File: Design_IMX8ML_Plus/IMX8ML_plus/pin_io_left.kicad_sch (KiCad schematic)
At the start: 4 parts, among them J1 Back_Right, J2 Front_Right

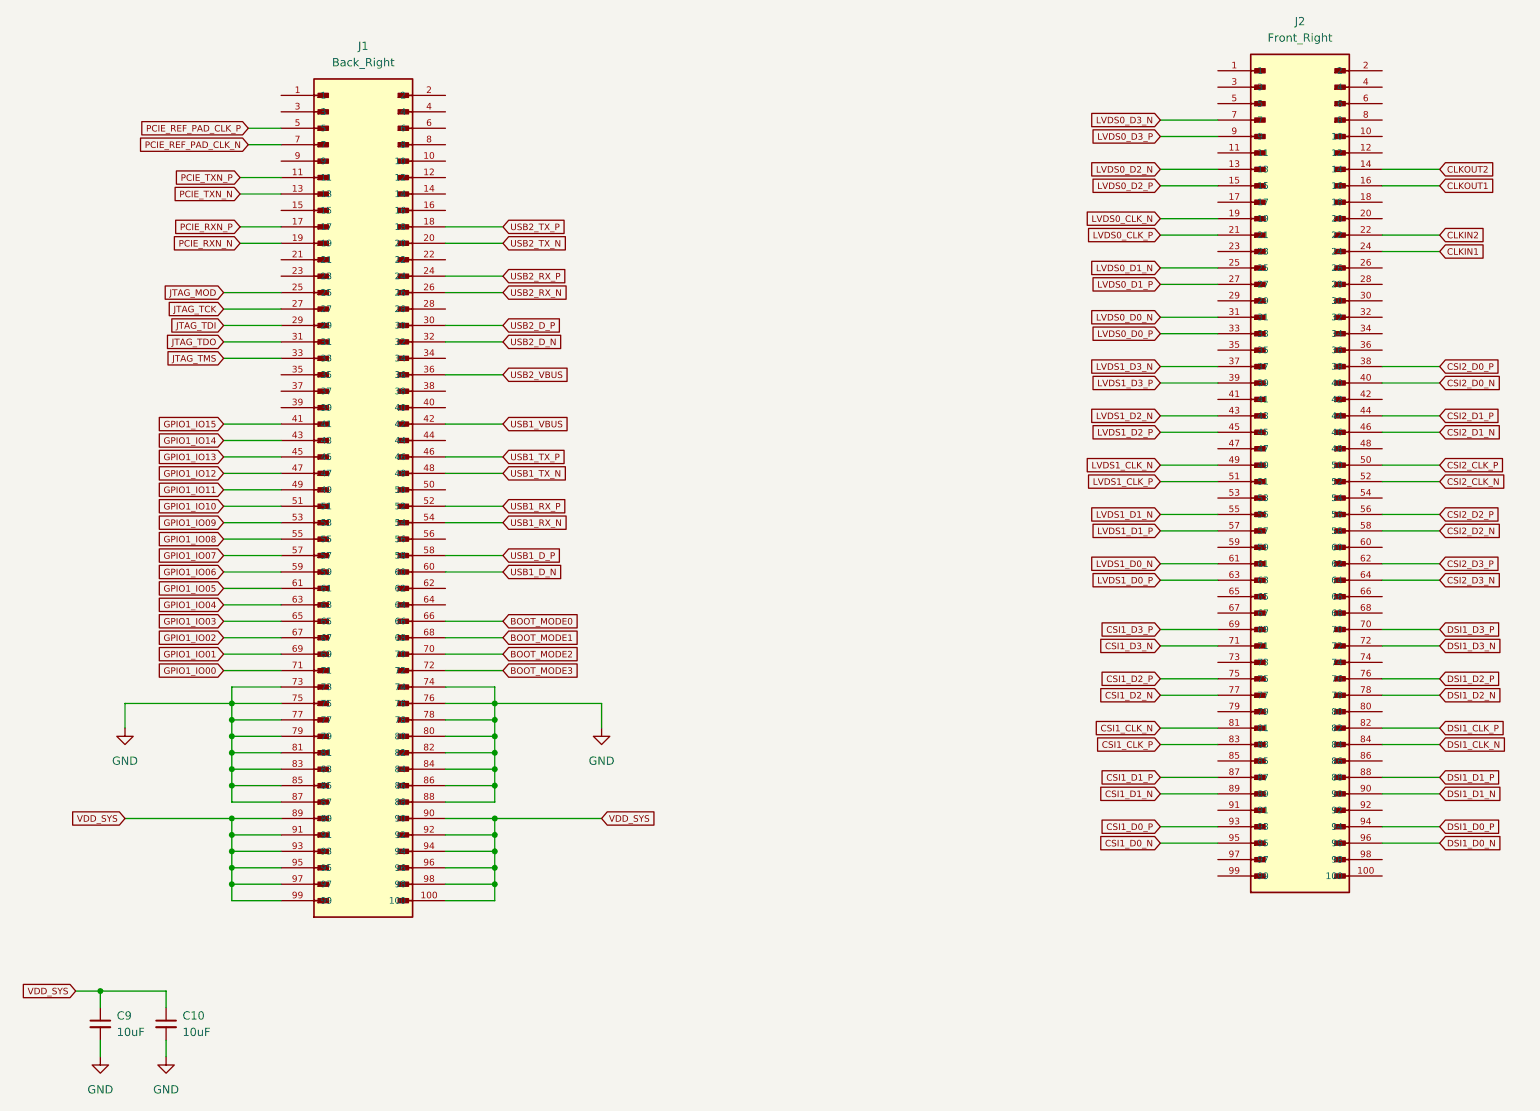
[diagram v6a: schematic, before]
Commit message: [PROCESSOR] Create zones It added power zones in the four layer
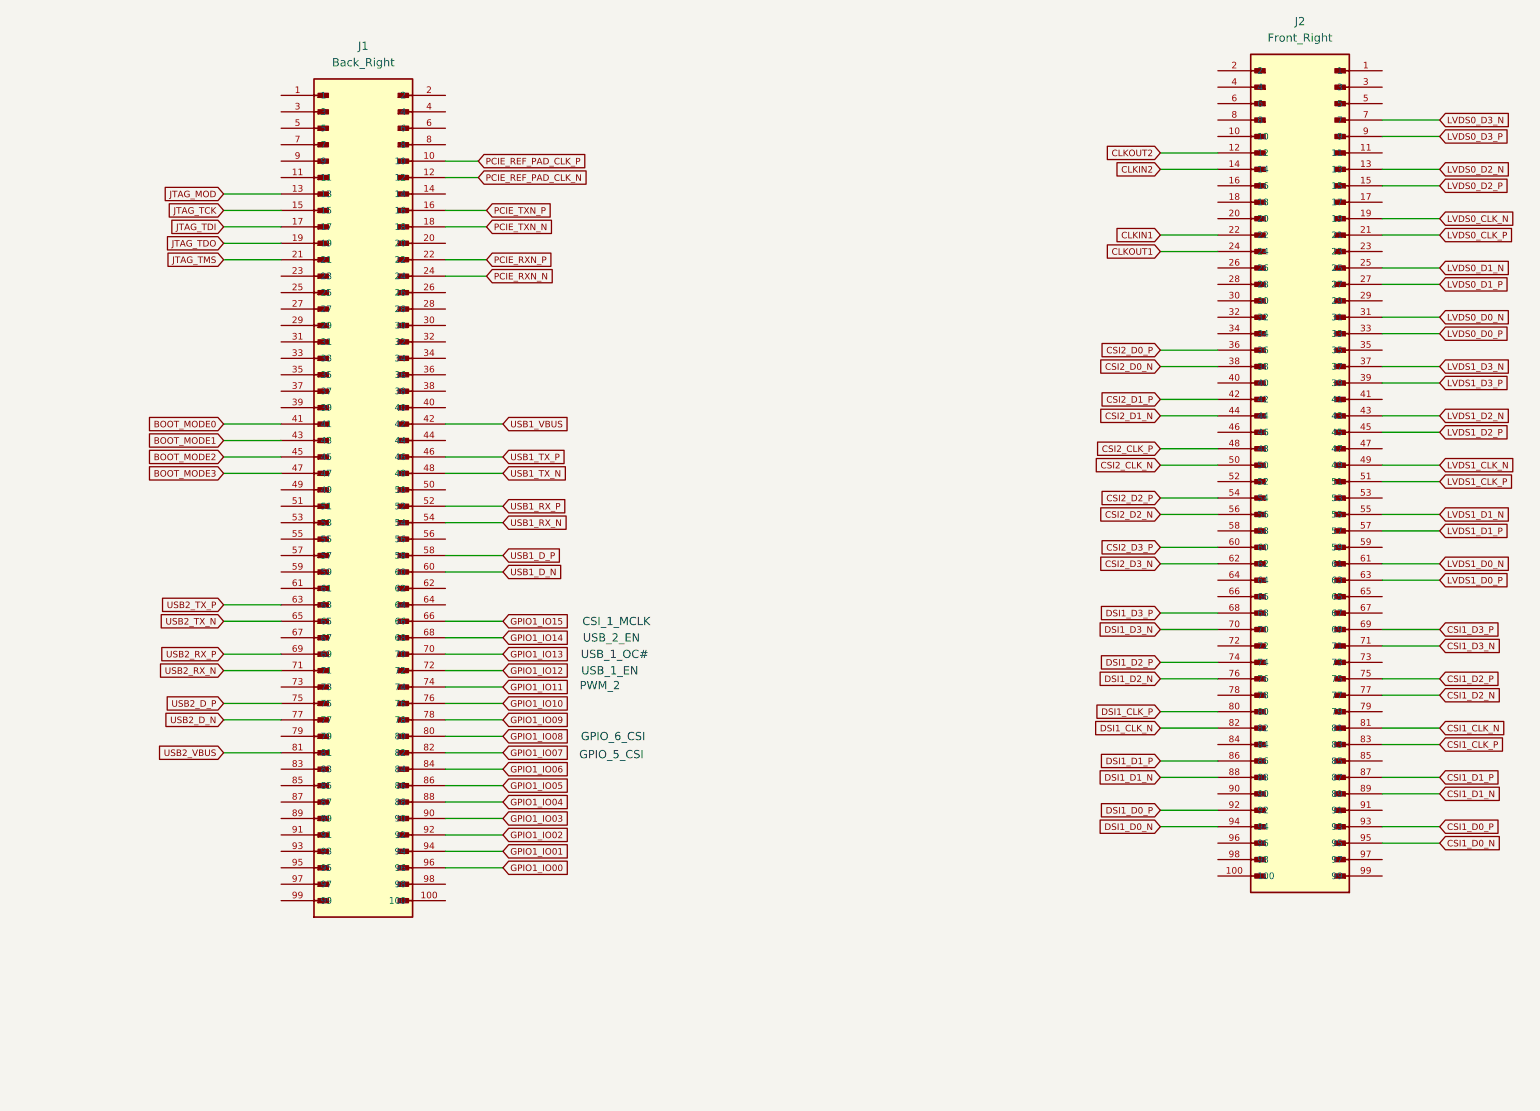
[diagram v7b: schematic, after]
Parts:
- removed C10, C9: 10uF, Capacitor_SMD:C_0201_0603Metric_Pad0.64x0.40mm_HandSolder, symbol Device:C_Small
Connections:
- net BOOT_MODE0: now also J1.41; no longer J1.66
- net BOOT_MODE1: now also J1.43; no longer J1.68
- net BOOT_MODE2: now also J1.45; no longer J1.70
- net BOOT_MODE3: now also J1.47; no longer J1.72
- net CLKIN1: now also J2.22; no longer J2.24
- net CLKIN2: now also J2.14; no longer J2.22
- net CLKOUT1: now also J2.24; no longer J2.16
- net CLKOUT2: now also J2.12; no longer J2.14
- net CSI2_CLK_N: now also J2.50; no longer J2.52
- net CSI2_CLK_P: now also J2.48; no longer J2.50
- net CSI2_D0_N: now also J2.38; no longer J2.40
- net CSI2_D0_P: now also J2.36; no longer J2.38
- net CSI2_D1_N: now also J2.44; no longer J2.46
- net CSI2_D1_P: now also J2.42; no longer J2.44
- net CSI2_D2_N: now also J2.56; no longer J2.58
- net CSI2_D2_P: now also J2.54; no longer J2.56
- net CSI2_D3_N: now also J2.62; no longer J2.64
- net CSI2_D3_P: now also J2.60; no longer J2.62
- net DSI1_CLK_N: now also J2.82; no longer J2.84
- net DSI1_CLK_P: now also J2.80; no longer J2.82
- net DSI1_D0_N: now also J2.94; no longer J2.96
- net DSI1_D0_P: now also J2.92; no longer J2.94
- net DSI1_D1_N: now also J2.88; no longer J2.90
- net DSI1_D1_P: now also J2.86; no longer J2.88
- net DSI1_D2_N: now also J2.76; no longer J2.78
- net DSI1_D2_P: now also J2.74; no longer J2.76
- net DSI1_D3_N: now also J2.70; no longer J2.72
- net DSI1_D3_P: now also J2.68; no longer J2.70
- net GPIO1_IO00: now also J1.96; no longer J1.71
- net GPIO1_IO01: now also J1.94; no longer J1.69
- net GPIO1_IO02: now also J1.92; no longer J1.67
- net GPIO1_IO03: now also J1.90; no longer J1.65
- net GPIO1_IO04: now also J1.88; no longer J1.63
- net GPIO1_IO05: now also J1.86; no longer J1.61
- net GPIO1_IO06: now also J1.84; no longer J1.59
- net GPIO1_IO07: now also J1.82; no longer J1.57
- net GPIO1_IO08: now also J1.80; no longer J1.55
- net GPIO1_IO09: now also J1.78; no longer J1.53
- net GPIO1_IO10: now also J1.76; no longer J1.51
- net GPIO1_IO11: now also J1.74; no longer J1.49
- net GPIO1_IO12: now also J1.72; no longer J1.47
- net GPIO1_IO13: now also J1.70; no longer J1.45
- net GPIO1_IO14: now also J1.68; no longer J1.43
- net GPIO1_IO15: now also J1.66; no longer J1.41
- net JTAG_MOD: now also J1.13; no longer J1.25
- net JTAG_TCK: now also J1.15; no longer J1.27
- net JTAG_TDI: now also J1.17; no longer J1.29
- net JTAG_TDO: now also J1.19; no longer J1.31
- net JTAG_TMS: now also J1.21; no longer J1.33
- net PCIE_REF_PAD_CLK_N: now also J1.12; no longer J1.7
- net PCIE_REF_PAD_CLK_P: now also J1.10; no longer J1.5
- net PCIE_RXN_N: now also J1.24; no longer J1.19
- net PCIE_RXN_P: now also J1.22; no longer J1.17
- net PCIE_TXN_N: now also J1.18; no longer J1.13
- net PCIE_TXN_P: now also J1.16; no longer J1.11
- net USB2_D_N: now also J1.77; no longer J1.32
- net USB2_D_P: now also J1.75; no longer J1.30
- net USB2_RX_N: now also J1.71; no longer J1.26
- net USB2_RX_P: now also J1.69; no longer J1.24
- net USB2_TX_N: now also J1.65; no longer J1.20
- net USB2_TX_P: now also J1.63; no longer J1.18
- net USB2_VBUS: now also J1.81; no longer J1.36
- removed net GND: J1.73, J1.74, J1.75, J1.76, J1.77, J1.78, J1.79, J1.80, J1.81, J1.82, J1.83, J1.84, J1.85, J1.86, J1.87, J1.88
- removed net VDD_SYS: J1.100, J1.89, J1.90, J1.91, J1.92, J1.93, J1.94, J1.95, J1.96, J1.97, J1.98, J1.99
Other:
- note added: "CSI_1_MCLK"
- note added: "GPIO_5_CSI"
- note added: "GPIO_6_CSI"
- note added: "PWM_2"
- note added: "USB_1_EN"
- note added: "USB_1_OC#"
- note added: "USB_2_EN"

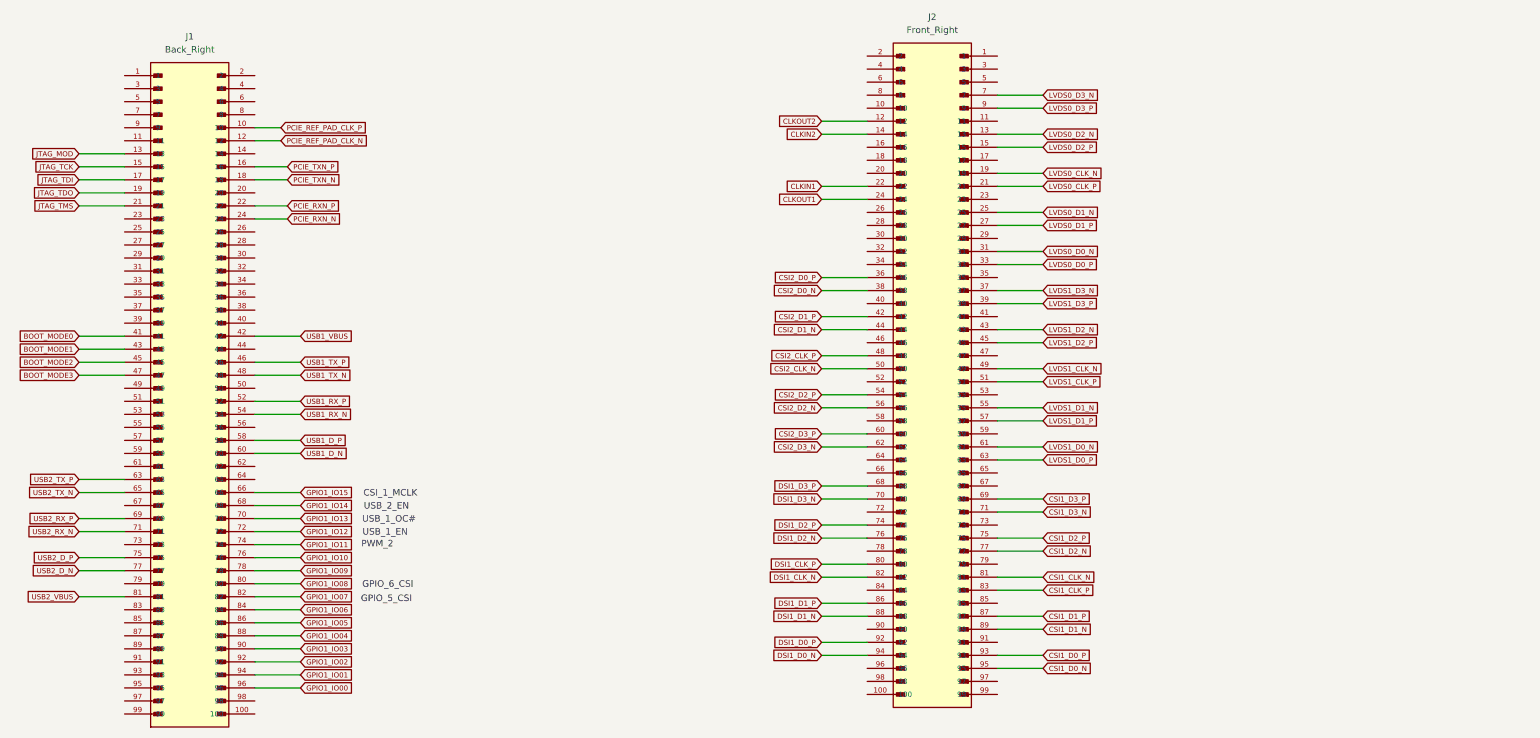
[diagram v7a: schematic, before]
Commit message: [CPU/BB] Improving the conection between the cpu and BB
* Reorganization of the components in the Base board.
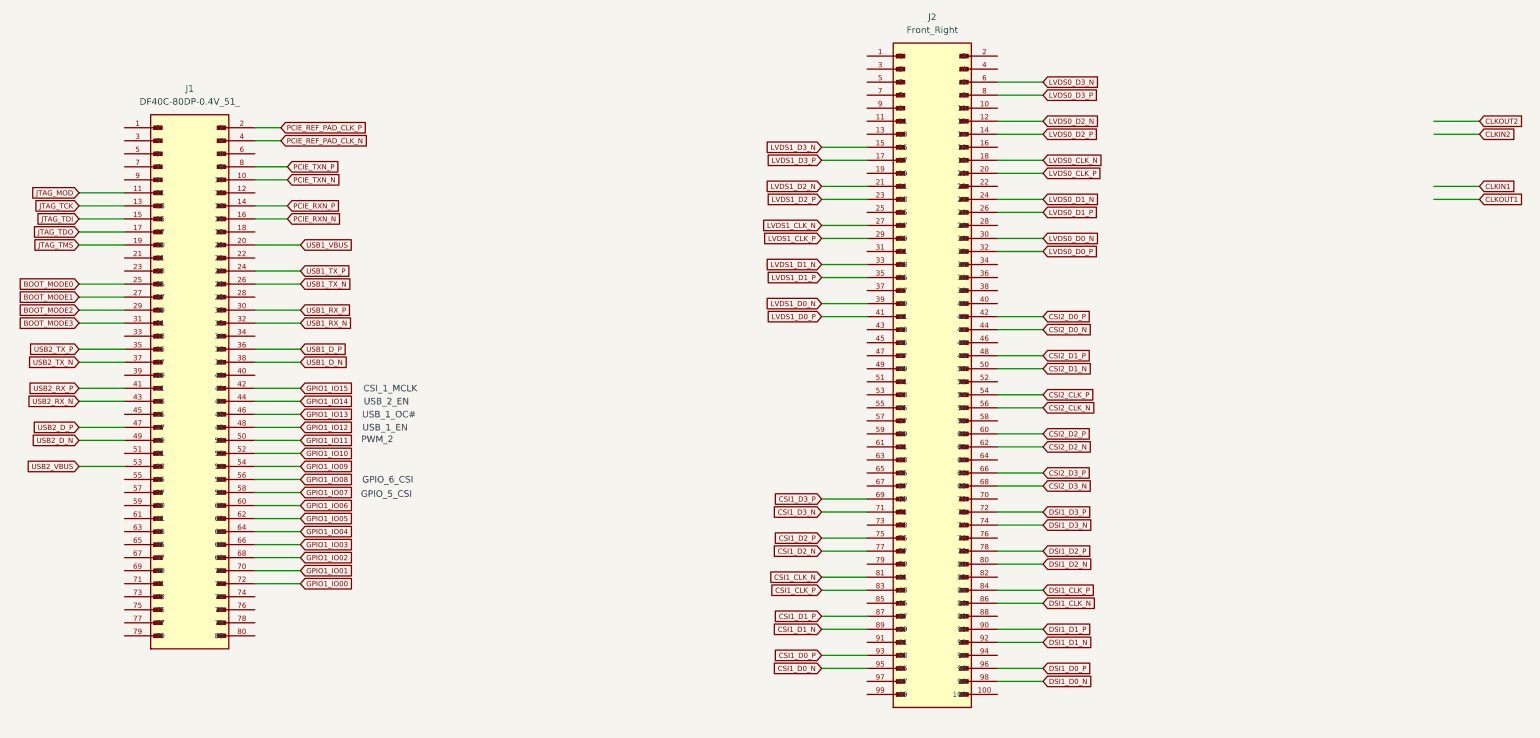
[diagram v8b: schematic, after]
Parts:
- removed J1: Back_Right, _W_SBC:HIROSE_DF40C-100DS-0.4V_51_, symbol CONN_DF40C-100DS-0_4V51_HIR:DF40C-100DP-0.4V_51_
- added J1: DF40C-80DP-0.4V_51_, _W_SBC:HRS_DF40C-80DS-0.4V_51_, symbol DF40C-80DP-0.4V_51_:DF40C-80DP-0.4V_51_
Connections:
- net BOOT_MODE0: now also J1.25
- net BOOT_MODE1: now also J1.27
- net BOOT_MODE2: now also J1.29
- net BOOT_MODE3: now also J1.31
- net CLKIN1: no longer J2.22
- net CLKIN2: no longer J2.14
- net CLKOUT1: no longer J2.24
- net CLKOUT2: no longer J2.12
- net CSI2_CLK_N: now also J2.56; no longer J2.50
- net CSI2_CLK_P: now also J2.54; no longer J2.48
- net CSI2_D0_N: now also J2.44; no longer J2.38
- net CSI2_D0_P: now also J2.42; no longer J2.36
- net CSI2_D1_N: now also J2.50; no longer J2.44
- net CSI2_D1_P: now also J2.48; no longer J2.42
- net CSI2_D2_N: now also J2.62; no longer J2.56
- net CSI2_D2_P: now also J2.60; no longer J2.54
- net CSI2_D3_N: now also J2.68; no longer J2.62
- net CSI2_D3_P: now also J2.66; no longer J2.60
- net DSI1_CLK_N: now also J2.86; no longer J2.82
- net DSI1_CLK_P: now also J2.84; no longer J2.80
- net DSI1_D0_N: now also J2.98; no longer J2.94
- net DSI1_D0_P: now also J2.96; no longer J2.92
- net DSI1_D1_N: now also J2.92; no longer J2.88
- net DSI1_D1_P: now also J2.90; no longer J2.86
- net DSI1_D2_N: now also J2.80; no longer J2.76
- net DSI1_D2_P: now also J2.78; no longer J2.74
- net DSI1_D3_N: now also J2.74; no longer J2.70
- net DSI1_D3_P: now also J2.72; no longer J2.68
- net GPIO1_IO00: now also J1.72
- net GPIO1_IO01: now also J1.70
- net GPIO1_IO02: now also J1.68
- net GPIO1_IO03: now also J1.66
- net GPIO1_IO04: now also J1.64
- net GPIO1_IO05: now also J1.62
- net GPIO1_IO06: now also J1.60
- net GPIO1_IO07: now also J1.58
- net GPIO1_IO08: now also J1.56
- net GPIO1_IO09: now also J1.54
- net GPIO1_IO10: now also J1.52
- net GPIO1_IO11: now also J1.50
- net GPIO1_IO12: now also J1.48
- net GPIO1_IO13: now also J1.46
- net GPIO1_IO14: now also J1.44
- net GPIO1_IO15: now also J1.42
- net JTAG_MOD: now also J1.11
- net JTAG_TCK: now also J1.13
- net JTAG_TDI: now also J1.15
- net JTAG_TDO: now also J1.17
- net JTAG_TMS: now also J1.19
- net LVDS0_CLK_N: now also J2.18; no longer J2.19
- net LVDS0_CLK_P: now also J2.20; no longer J2.21
- net LVDS0_D0_N: now also J2.30; no longer J2.31
- net LVDS0_D0_P: now also J2.32; no longer J2.33
- net LVDS0_D1_N: now also J2.24; no longer J2.25
- net LVDS0_D1_P: now also J2.26; no longer J2.27
- net LVDS0_D2_N: now also J2.12; no longer J2.13
- net LVDS0_D2_P: now also J2.14; no longer J2.15
- net LVDS0_D3_N: now also J2.6; no longer J2.7
- net LVDS0_D3_P: now also J2.8; no longer J2.9
- net LVDS1_CLK_N: now also J2.27; no longer J2.49
- net LVDS1_CLK_P: now also J2.29; no longer J2.51
- net LVDS1_D0_N: now also J2.39; no longer J2.61
- net LVDS1_D0_P: now also J2.41; no longer J2.63
- net LVDS1_D1_N: now also J2.33; no longer J2.55
- net LVDS1_D1_P: now also J2.35; no longer J2.57
- net LVDS1_D2_N: now also J2.21; no longer J2.43
- net LVDS1_D2_P: now also J2.23; no longer J2.45
- net LVDS1_D3_N: now also J2.15; no longer J2.37
- net LVDS1_D3_P: now also J2.17; no longer J2.39
- net PCIE_REF_PAD_CLK_N: now also J1.4
- net PCIE_REF_PAD_CLK_P: now also J1.2
- net PCIE_RXN_N: now also J1.16
- net PCIE_RXN_P: now also J1.14
- net PCIE_TXN_N: now also J1.10
- net PCIE_TXN_P: now also J1.8
- net USB1_D_N: now also J1.38
- net USB1_D_P: now also J1.36
- net USB1_RX_N: now also J1.32
- net USB1_RX_P: now also J1.30
- net USB1_TX_N: now also J1.26
- net USB1_TX_P: now also J1.24
- net USB1_VBUS: now also J1.20
- net USB2_D_N: now also J1.49
- net USB2_D_P: now also J1.47
- net USB2_RX_N: now also J1.43
- net USB2_RX_P: now also J1.41
- net USB2_TX_N: now also J1.37
- net USB2_TX_P: now also J1.35
- net USB2_VBUS: now also J1.53
